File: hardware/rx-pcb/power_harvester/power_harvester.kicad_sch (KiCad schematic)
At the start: 5 parts, among them J1 Conn_Coaxial_Small

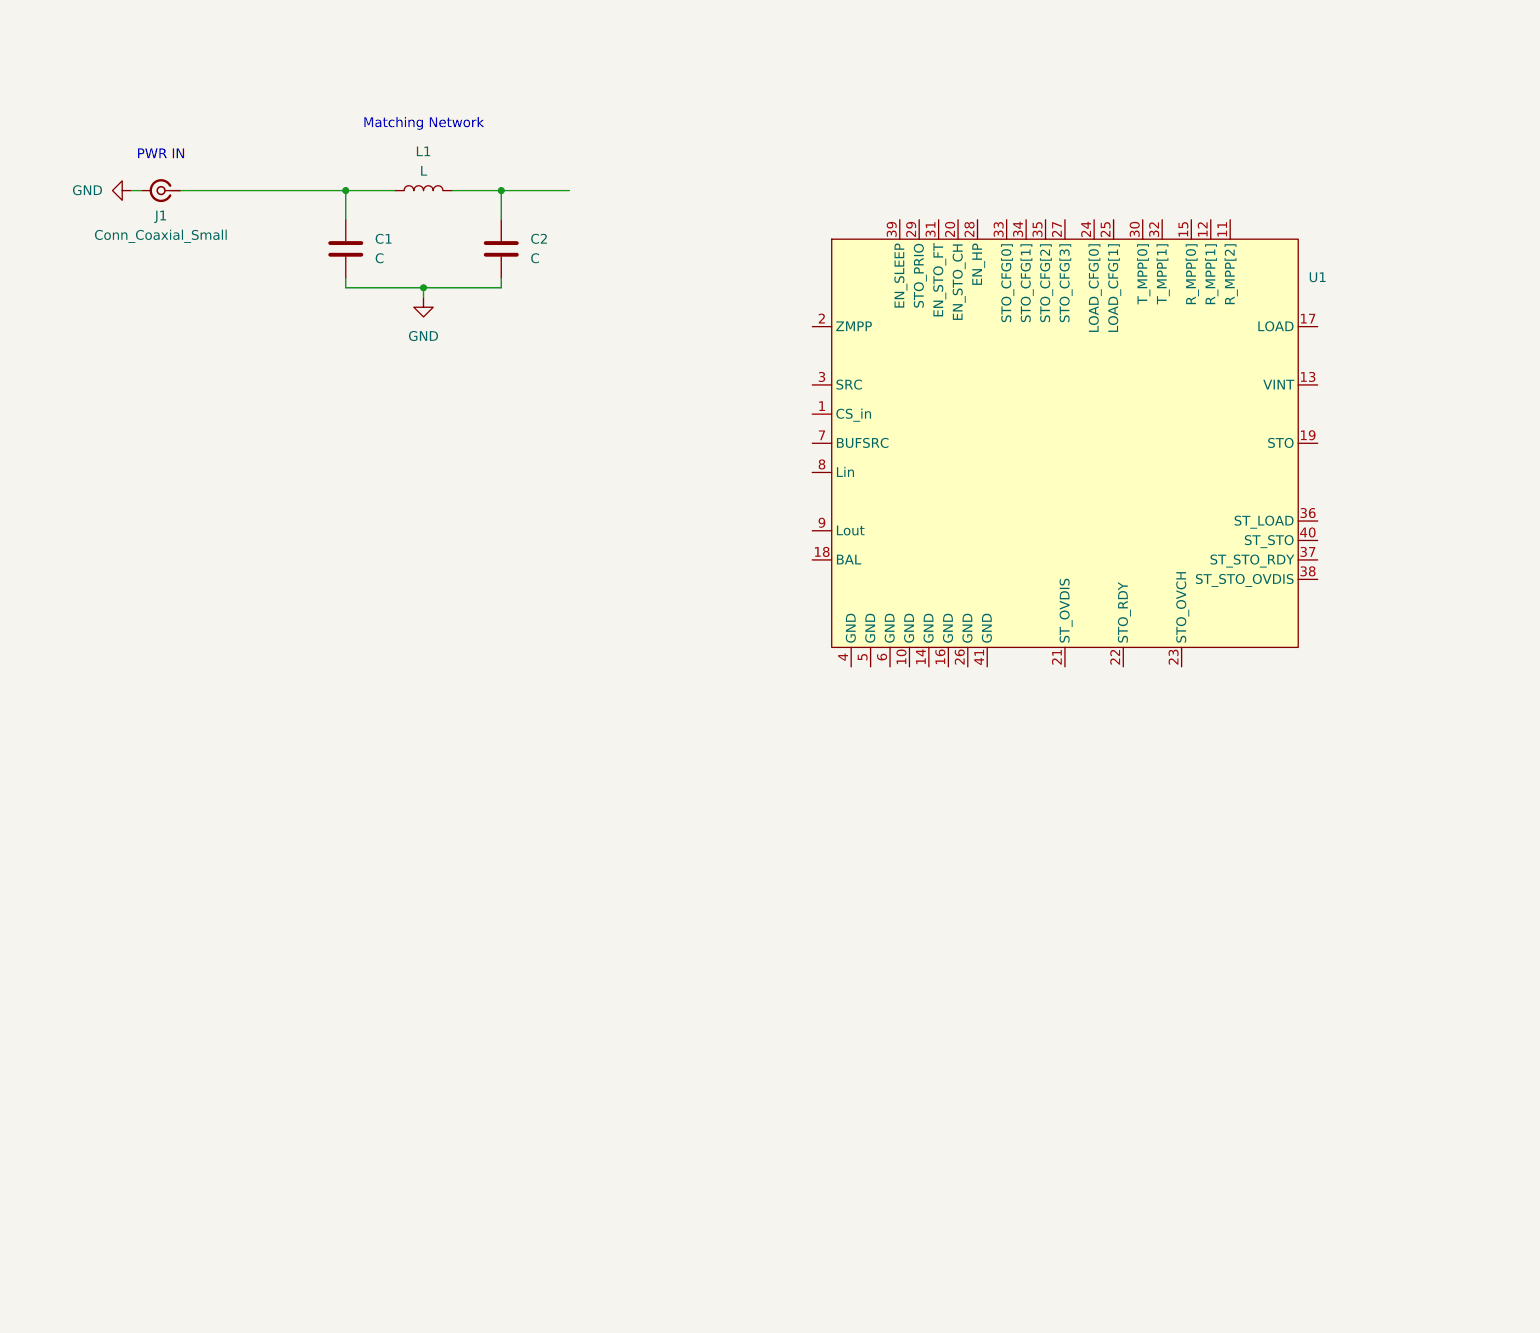
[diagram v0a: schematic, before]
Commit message: updated energy harvesting IC. Configured it based on the datasheet for this application. Waiting on capacitor bank decision.
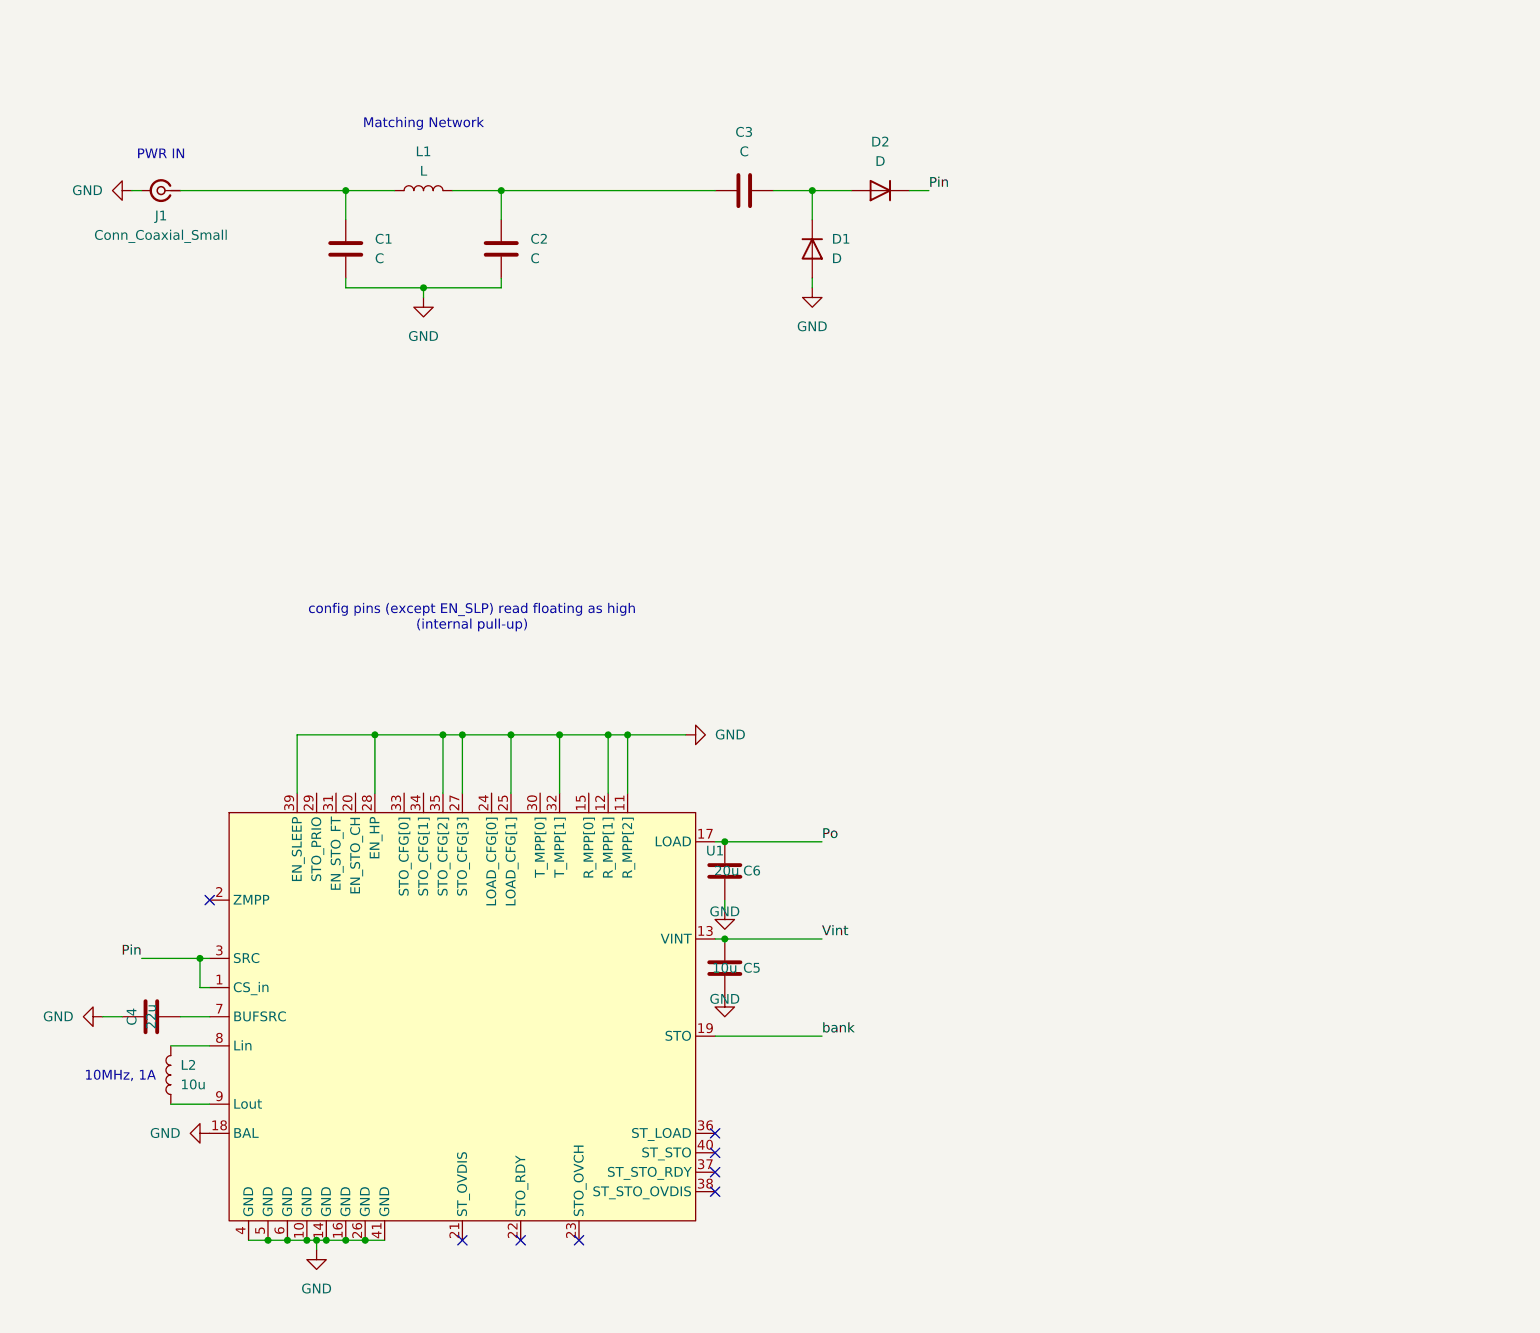
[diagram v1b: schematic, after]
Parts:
- added C3: C, Capacitor_SMD:C_0805_2012Metric_Pad1.18x1.45mm_HandSolder, symbol Device:C
- added C4: 22u, Capacitor_SMD:C_0805_2012Metric_Pad1.18x1.45mm_HandSolder, symbol Device:C
- added C5: 10u, Capacitor_SMD:C_0805_2012Metric_Pad1.18x1.45mm_HandSolder, symbol Device:C
- added C6: 20u, Capacitor_SMD:C_0805_2012Metric_Pad1.18x1.45mm_HandSolder, symbol Device:C
- added D1, D2: D, symbol Device:D
- added L2: 10u, symbol Device:L
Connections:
- net GND: now also U1.10 (GND), U1.11 (R_MPP[2]), U1.12 (R_MPP[1]), U1.14 (GND), U1.16 (GND), U1.18 (BAL), U1.25 (LOAD_CFG[1]), U1.26 (GND), U1.27 (STO_CFG[3]), U1.28 (EN_HP), U1.32 (T_MPP[1]), U1.35 (STO_CFG[2]), U1.39 (EN_SLEEP), U1.4 (GND), U1.41 (GND), U1.5 (GND), U1.6 (GND), C4.1, C5.1, C6.1, D1.2 (A)
- net at C2.1, L1.2: now also C3.1
- net Pin: now reaches U1.1 (CS_in)
- net Pin: now also U1.3 (SRC), D2.1 (K)
- net Vint: now reaches U1.13 (VINT)
- net Vint: now also C5.2
- net Po: now reaches U1.17 (LOAD)
- net Po: now also C6.2
- net bank: now reaches U1.19 (STO)
- net at U1.7 (BUFSRC): now also C4.2
- net at U1.8 (Lin): now also L2.2
- net at U1.9 (Lout): now also L2.1
- new net: C3.2, D1.1 (K), D2.2 (A)
- no-connect marks 0 -> 8
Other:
- note added: "10MHz, 1A"
- note added: "config pins (except EN_SLP) read floating as high (internal pull-up)"
- moved on the sheet: U1

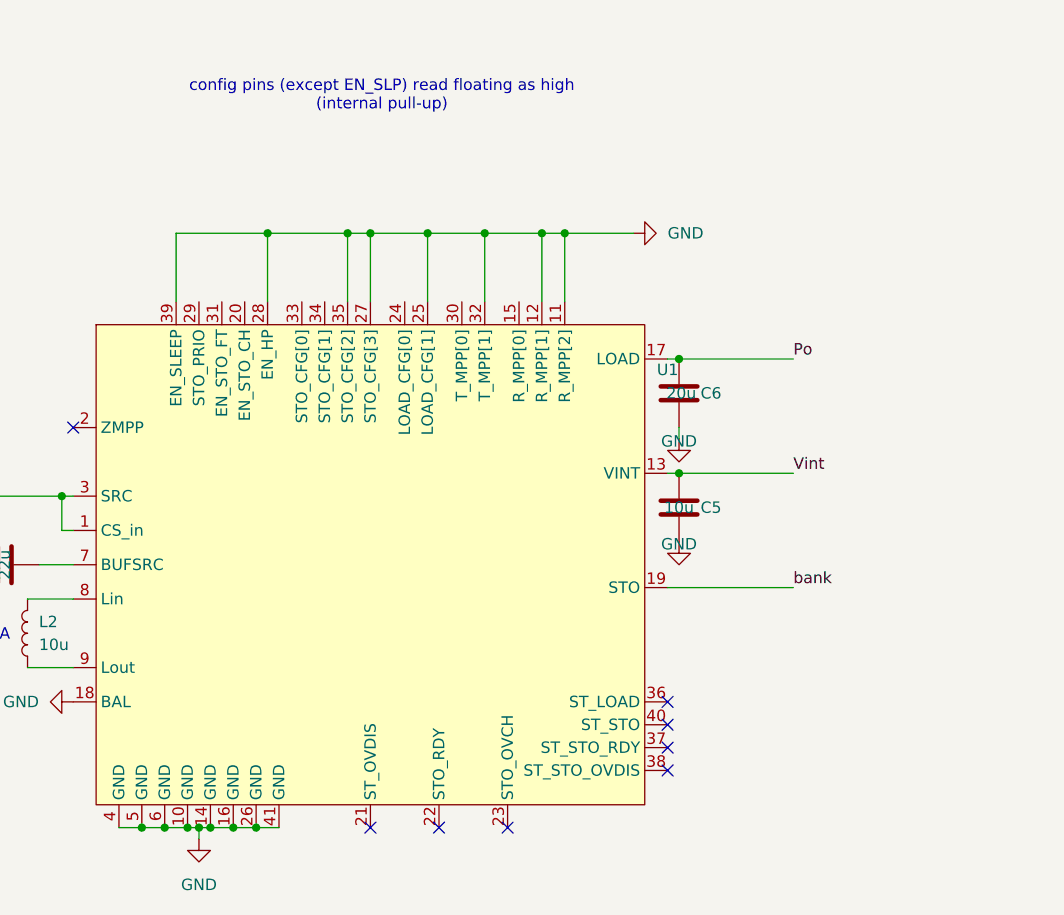
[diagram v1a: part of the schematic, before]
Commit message: added selected diodes and bank capacitor. began board layout.
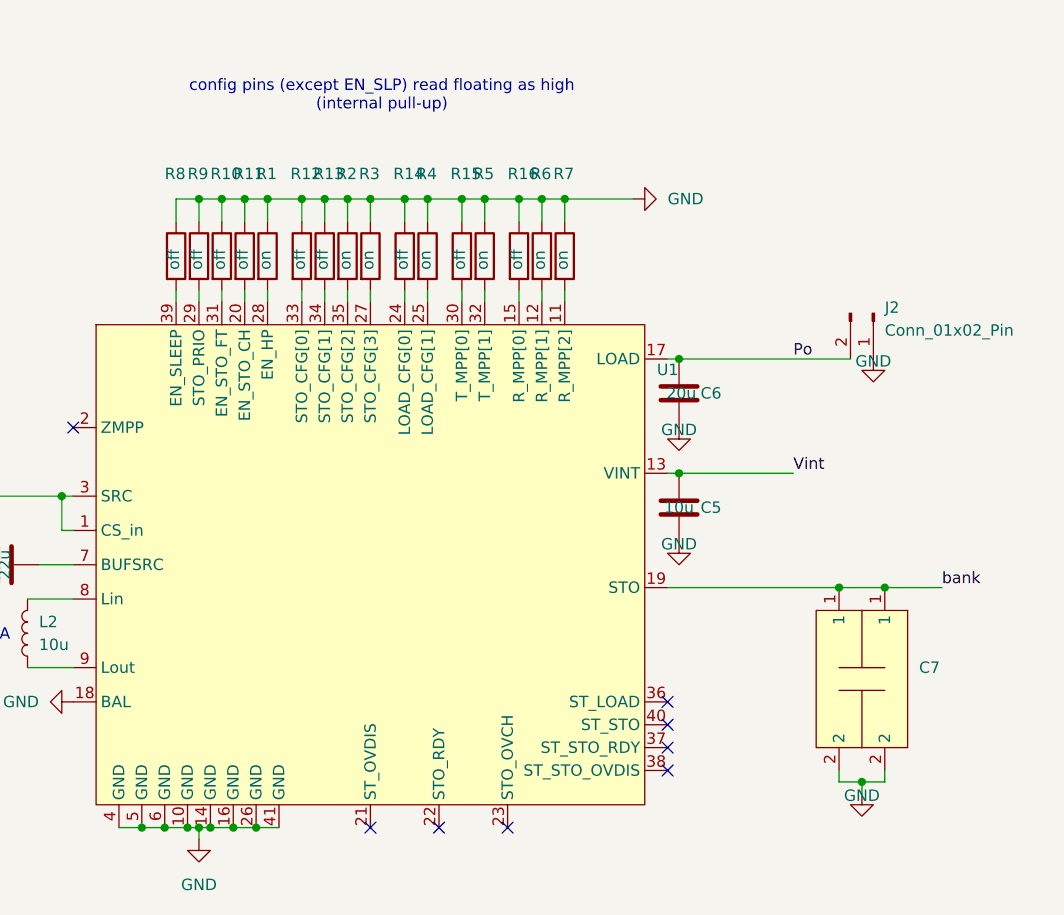
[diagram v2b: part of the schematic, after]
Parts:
- added C7: ~, power_harvester:C4AQXEXXXXXXXAX, symbol power_harvester:C4AQXEXXXXXXXAX
- added J2: Conn_01x02_Pin, Connector_PinHeader_2.54mm:PinHeader_1x02_P2.54mm_Vertical, symbol Connector:Conn_01x02_Pin
- added R1, R2, R3, R4, R5, R6, R7: on, Resistor_SMD:R_0201_0603Metric, symbol Device:R
- added R10, R11, R12, R13, R14, R15, R16, R8, R9: off, Resistor_SMD:R_0201_0603Metric, symbol Device:R
- D1, D2: footprint (none) -> power_harvester:JDH2S02SL
- L2: footprint (none) -> power_harvester:WE-MAPI
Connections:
- net GND: now also C7.2, J2.1 (Pin_1), R1.1, R10.1, R11.1, R12.1, R13.1, R14.1, R15.1, R16.1, R2.1, R3.1, R4.1, R5.1, R6.1, R7.1, R8.1, R9.1; no longer U1.11 (R_MPP[2]), U1.12 (R_MPP[1]), U1.25 (LOAD_CFG[1]), U1.27 (STO_CFG[3]), U1.28 (EN_HP), U1.32 (T_MPP[1]), U1.35 (STO_CFG[2]), U1.39 (EN_SLEEP)
- net Po: now also J2.2 (Pin_2)
- net bank: now also C7.1
- net at U1.15 (R_MPP[0]): now also R16.2
- net at U1.20 (EN_STO_CH): now also R11.2
- net at U1.24 (LOAD_CFG[0]): now also R14.2
- net at U1.29 (STO_PRIO): now also R9.2
- net at U1.30 (T_MPP[0]): now also R15.2
- net at U1.31 (EN_STO_FT): now also R10.2
- net at U1.33 (STO_CFG[0]): now also R12.2
- net at U1.34 (STO_CFG[1]): now also R13.2
- new net: R7.2, U1.11 (R_MPP[2])
- new net: R8.2, U1.39 (EN_SLEEP)
- new net: R6.2, U1.12 (R_MPP[1])
- new net: R4.2, U1.25 (LOAD_CFG[1])
- new net: R3.2, U1.27 (STO_CFG[3])
- new net: R1.2, U1.28 (EN_HP)
- new net: R5.2, U1.32 (T_MPP[1])
- new net: R2.2, U1.35 (STO_CFG[2])
